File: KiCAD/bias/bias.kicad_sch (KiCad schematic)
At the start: 59 parts, among them J11 GRID_BIAS, J12 CATHODE_SENSE, J14 Conn_01x02_Pin, J3 Conn_01x02_Pin, Q2 2N7000, Q3 2N7000, U10 OPA454, U11 LM4040LP-5, U12 LM393, U13 OPA1641, U14 OPA1641, U5 OPA454, U9 LM7805_TO220

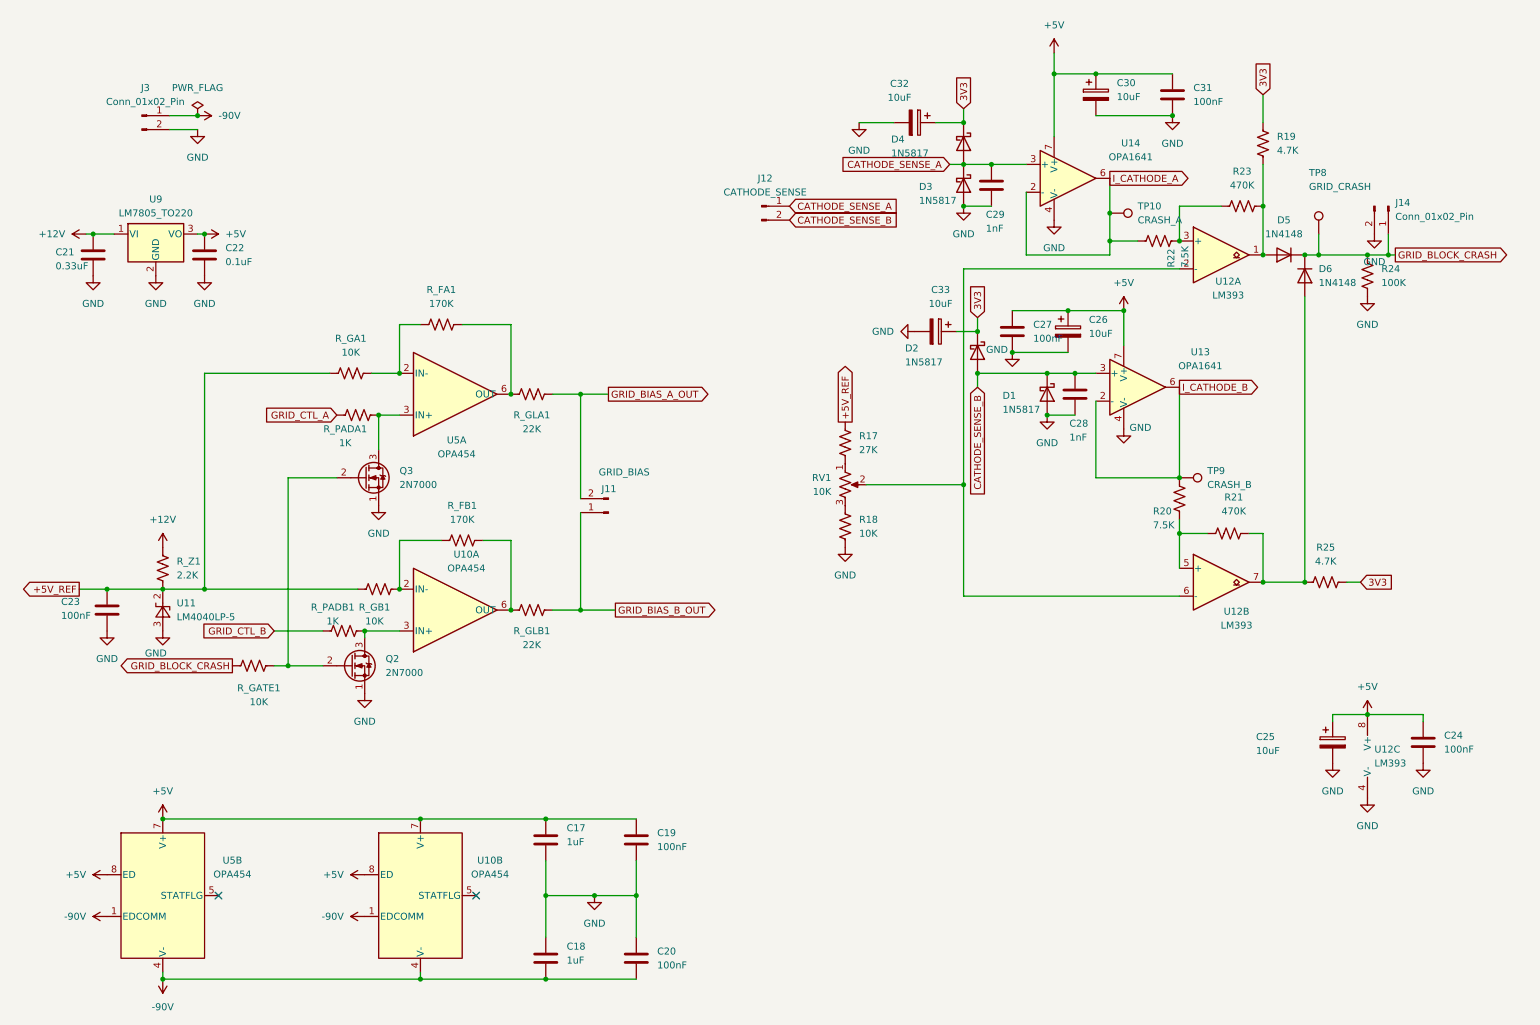
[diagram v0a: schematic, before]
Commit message: revB: bias supply redesign + schematic edits
OPA454 supply: V+ +5V → +12V, V− −90V → −75V (87V total, 13V margin
from 100V abs max). R_FA/R_FB: 170kΩ → 140kΩ. Transfer function:
V_out = V_DAC×15−70. IDLE: −85V → −70V. OPERATE V_DAC: 1.94V → 1.333V
(DAC code ~1092). V− supply: 262F12 120VAC secondary + bridge rectifier
+ 1N5372B (75V/5W) + 5.6kΩ/2W. Updated grid_bias.md,
2026-06-08-pa-validation.md, pa_cathode_monitor.md throughout.
KiCad: bias.kicad_sch and arduino.kicad_sch schematic edits.

Co-Authored-By: Claude Sonnet 4.6 <noreply@anthropic.com>
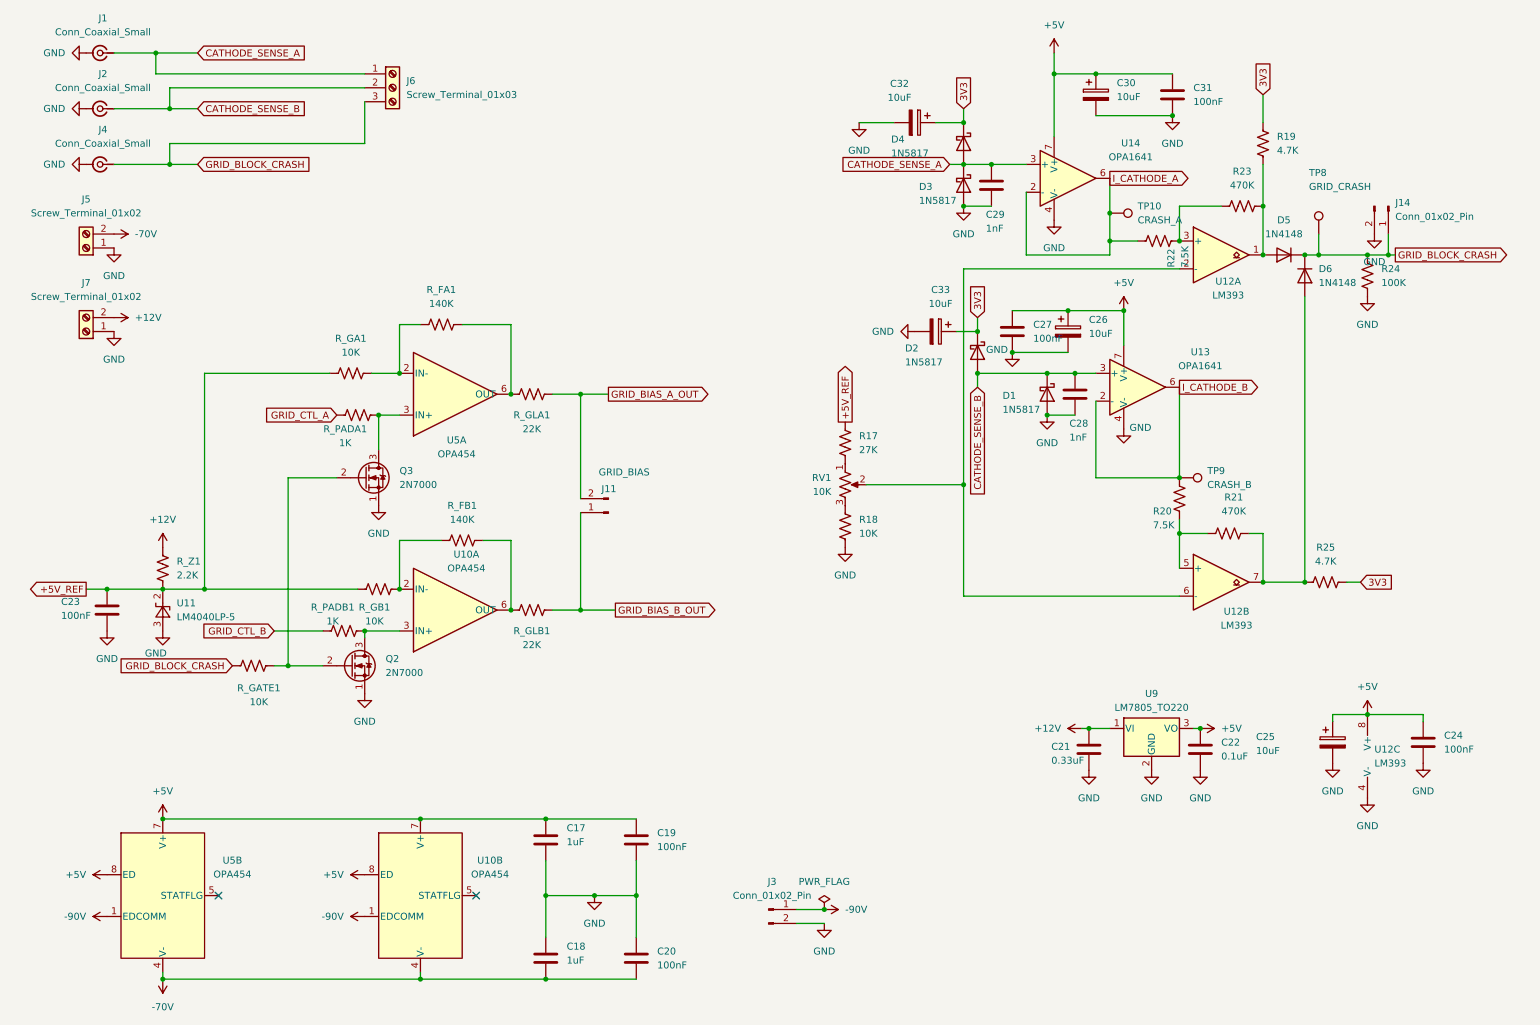
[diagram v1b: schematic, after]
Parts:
- removed J12: CATHODE_SENSE, Connector_PinHeader_2.54mm:PinHeader_1x02_P2.54mm_Vertical, symbol Connector:Conn_01x02_Pin
- added J1, J2, J4: Conn_Coaxial_Small, symbol Connector:Conn_Coaxial_Small
- added J5, J7: Screw_Terminal_01x02, symbol Connector:Screw_Terminal_01x02
- added J6: Screw_Terminal_01x03, symbol Connector:Screw_Terminal_01x03
- R_FA1, R_FB1: value 170K -> 140K
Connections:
- net +12V: now also J7.2 (Pin_2)
- net -90V: no longer C18.2, C20.2, U10.4 (V-), U5.4 (V-)
- net CATHODE_SENSE_A: now also J1.1 (In), J6.1 (Pin_1)
- net CATHODE_SENSE_B: now also J2.1 (In), J6.2 (Pin_2)
- net GND: now also J1.2 (Ext), J2.2 (Ext), J4.2 (Ext), J5.1 (Pin_1), J7.1 (Pin_1)
- net GRID_BLOCK_CRASH: now also J4.1 (In), J6.3 (Pin_3)
- new net -70V: C18.2, C20.2, J5.2 (Pin_2), U10.4 (V-), U5.4 (V-)
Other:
- moved on the sheet: C21, C22, J3, U9

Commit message: KiCad revB: schematic fixes on analog + bias boards
Fix ERC errors and connectivity issues: GRID_BLOCK_CRASH label
direction, GRID_CTL_A/B board boundary wiring, 3V3 source on bias
board. New ERC error on bias board still open (to be fixed next).

Co-Authored-By: Claude Sonnet 4.6 <noreply@anthropic.com>
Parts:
- removed J14, J3: Conn_01x02_Pin, Connector_PinHeader_2.54mm:PinHeader_1x02_P2.54mm_Vertical, symbol Connector:Conn_01x02_Pin
- removed J6: Screw_Terminal_01x03, symbol Connector:Screw_Terminal_01x03
- added J3, J8: Screw_Terminal_01x02, symbol Connector:Screw_Terminal_01x02
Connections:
- net 3V3: no longer R19.1, R25.2
- net CATHODE_SENSE_A: now also J8.1 (Pin_1); no longer J1.1 (In)
- net CATHODE_SENSE_B: now also J8.2 (Pin_2); no longer J2.1 (In)
- net GND: now also J3.1 (Pin_1)
- net I_CATHODE_A: now also J1.1 (In)
- net I_CATHODE_B: now also J2.1 (In)
- new net +3.3V: J3.2 (Pin_2), R19.1, R25.2

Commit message: revB: arduino screw terminals + bias schematic edits; grid_bias.md updated for MCP4728 internal reference
Analog board arduino sheet: added screw terminal connections for all Metro GPIO
signals (PADDLE_A/B, I_CATHODE_A/B, GRID_BLOCK_CRASH, ENC_INT, MBL600_A/B).
Bias board: schematic edits (session work). grid_bias.md: corrected DAC codes
and rail voltages for MCP4728 internal 2.048V bandgap reference (OPERATE ~2667),
updated inter-sheet I/O references from MCP4725 to MCP4728.

Co-Authored-By: Claude Sonnet 4.6 <noreply@anthropic.com>
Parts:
- added C1, C2: 100nF, symbol Device:C_US
- added J6, J9: Conn_Coaxial_Small, symbol Connector:Conn_Coaxial_Small
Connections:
- net GND: now also C1.2, C2.2, J6.2 (Ext), J9.2 (Ext)
- net GRID_CTL_A: now also C2.1, J6.1 (In)
- net GRID_CTL_B: now also C1.1, J9.1 (In)

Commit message: KiCad revB: protoshield schematic complete + 1N4728A symbol + misc board edits
Protoshield (Metro ESP32-S3 GPIO signal conditioning):
- Full schematic drawn: series R + bypass C + Zener clamp for I_CATHODE_A/B
  (1k+100nF+1N4728A), MBL600_A/B (10k/20k divider + 22pF), GRID_BLOCK_CRASH
  (1k+100nF), ENC_INT (330R+10k pull-up), PADDLE_A/B (10k pull-ups), RESET_N
  (100nF), TR_SENSE (10k pull-up), passthrough nodes for SPI and LDAC_4728
- All THT footprints assigned (ceramic disc caps, DIN0207 resistors, Phoenix
  MKDS-1.5 2-pin/3-pin terminal blocks)
- ENC_INT wiring gap fixed (R7 re-placed to connect J4 pin 2 to ENC_INT net)
- sym-lib-table added (points to shared xmitter.kicad_sym)
- protoshield.net generated netlist added for reference

Symbol library (xmitter.kicad_sym):
- Added 1N4728A (3.3V 1W Zener, DO-41) with correct KiCad 9.0 inline pts format

Other boards:
- analog/arduino.kicad_sch: minor junction/reference adjustments after Metro
  symbol was removed to protoshield in prior session
- bias: kicad_pro and kicad_sch updated (ongoing schematic work)
- power/sym-lib-table added for new stub project

Added: Purchase Orders (JLCPCB + Digi-Key invoices), tools/_scan_symbols.py

Co-Authored-By: Claude Sonnet 4.6 <noreply@anthropic.com>
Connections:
- net 3V3 is gone; now on net +3.3V: C32.1, C33.1, D2.1 (K), D4.1 (K)
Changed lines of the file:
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@@
 		)
 	)
-	(global_label "3V3"
-		(shape input)
-		(at 184.15 30.48 90)
-		(fields_autoplaced yes)
-		(effects
-			(font
-				(size 1.27 1.27)
-			)
-			(justify left)
-		)
-		(property "Intersheetrefs" "${INTERSHEET_REFS}"
-			(at 184.15 23.9872 90)
-			(hide yes)
-			(show_name no)
-			(do_not_autoplace no)
-			(effects
-				(font
-					(size 1.27 1.27)
-				)
-				(justify left)
-			)
-		)
-	)
 	(global_label "I_CATHODE_B"
 		(shape output)
@@
 		)
 	)
-	(global_label "3V3"
-		(shape input)
-		(at 186.69 68.58 90)
-		(fields_autoplaced yes)
-		(effects
-			(font
-				(size 1.27 1.27)
-			)
-			(justify left)
-		)
-		(property "Intersheetrefs" "${INTERSHEET_REFS}"
-			(at 186.69 62.0872 90)
-			(hide yes)
-			(show_name no)
-			(do_not_autoplace no)
-			(effects
-				(font
-					(size 1.27 1.27)
-				)
-				(justify left)
-			)
-		)
-	)
 	(symbol
 		(lib_id "power:-90V")
@@
 	)
 	(symbol
+		(lib_id "power:+3.3V")
+		(at 186.69 68.58 0)
+		(unit 1)
+		(body_style 1)
+		(exclude_from_sim no)
+		(in_bom yes)
+		(on_board yes)
+		(in_pos_files yes)
+		(dnp no)
+		(fields_autoplaced yes)
+		(property "Reference" "#PWR017"
+			(at 186.69 72.39 0)
+			(hide yes)
+			(show_name no)
+			(do_not_autoplace no)
+			(effects
+				(font
+					(size 1.27 1.27)
+				)
+			)
+		)
+		(property "Value" "+3.3V"
+			(at 186.69 63.5 0)
+			(show_name no)
+			(do_not_autoplace no)
+			(effects
+				(font
+					(size 1.27 1.27)
+				)
+			)
+		)
+		(property "Footprint" ""
+			(at 186.69 68.58 0)
+			(hide yes)
+			(show_name no)
+			(do_not_autoplace no)
+			(effects
+				(font
+					(size 1.27 1.27)
+				)
+			)
+		)
+		(property "Datasheet" ""
+			(at 186.69 68.58 0)
+			(hide yes)
+			(show_name no)
+			(do_not_autoplace no)
+			(effects
+				(font
+					(size 1.27 1.27)
+				)
+			)
+		)
+		(property "Description" "Power symbol creates a global label with name \"+3.3V\""
+			(at 186.69 68.58 0)
+			(hide yes)
+			(show_name no)
+			(do_not_autoplace no)
+			(effects
+				(font
+					(size 1.27 1.27)
+				)
+			)
+		)
+		(pin "1"
+		)
+		(instances
+			(project "bias"
+				(path "/a692cd1f-3d9a-4c46-8d2f-b058d17ed461"
+					(reference "#PWR017")
+					(unit 1)
+				)
+			)
+		)
+	)
+	(symbol
 		(lib_id "power:+5V")
 		(at 227.33 143.51 270)
@@
 					(unit 1)
 				)
+			)
+		)
+	)
+	(symbol
+		(lib_id "power:+3.3V")
+		(at 184.15 30.48 0)
+		(unit 1)
+		(body_style 1)
+		(exclude_from_sim no)
+		(in_bom yes)
+		(on_board yes)
+		(in_pos_files yes)
+		(dnp no)
+		(fields_autoplaced yes)
+		(property "Reference" "#PWR016"
+			(at 184.15 34.29 0)
+			(hide yes)
+			(show_name no)
+			(do_not_autoplace no)
+			(effects
+				(font
+					(size 1.27 1.27)
+				)
+			)
+		)
+		(property "Value" "+3.3V"
+			(at 184.15 25.4 0)
+			(show_name no)
+			(do_not_autoplace no)
+			(effects
+				(font
+					(size 1.27 1.27)
+				)
+			)
+		)
+		(property "Footprint" ""
+			(at 184.15 30.48 0)
+			(hide yes)
+			(show_name no)
+			(do_not_autoplace no)
+			(effects
+				(font
+					(size 1.27 1.27)
+				)
+			)
+		)
+		(property "Datasheet" ""
+			(at 184.15 30.48 0)
+			(hide yes)
+			(show_name no)
+			(do_not_autoplace no)
+			(effects
+				(font
+					(size 1.27 1.27)
+				)
+			)
+		)
+		(property "Description" "Power symbol creates a global label with name \"+3.3V\""
+			(at 184.15 30.48 0)
+			(hide yes)
+			(show_name no)
+			(do_not_autoplace no)
+			(effects
+				(font
+					(size 1.27 1.27)
+				)
+			)
+		)
+		(pin "1"
+		)
+		(instances
+			(project "bias"
+				(path "/a692cd1f-3d9a-4c46-8d2f-b058d17ed461"
+					(reference "#PWR016")
+					(unit 1)
+				)
